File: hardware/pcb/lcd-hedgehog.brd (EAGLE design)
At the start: 24.4 x 27.4 mm, 22 parts

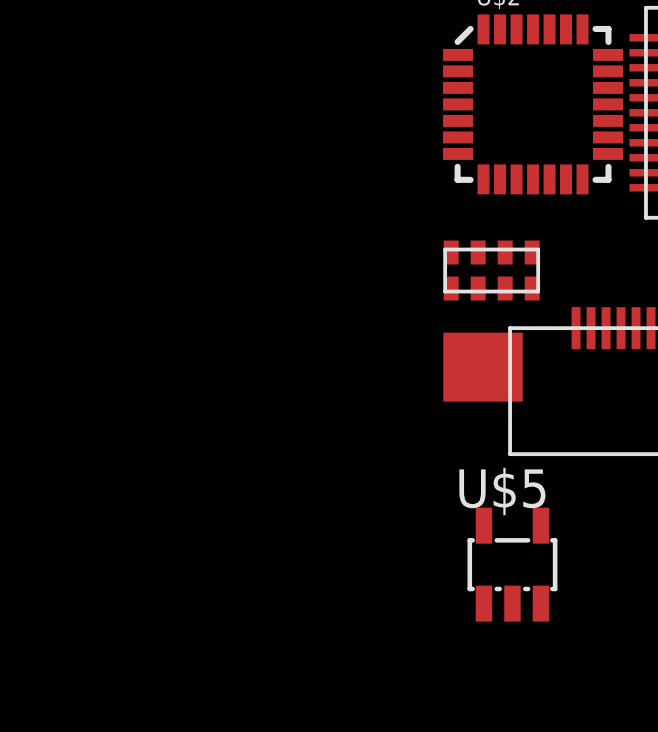
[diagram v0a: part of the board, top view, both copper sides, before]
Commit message: added ble
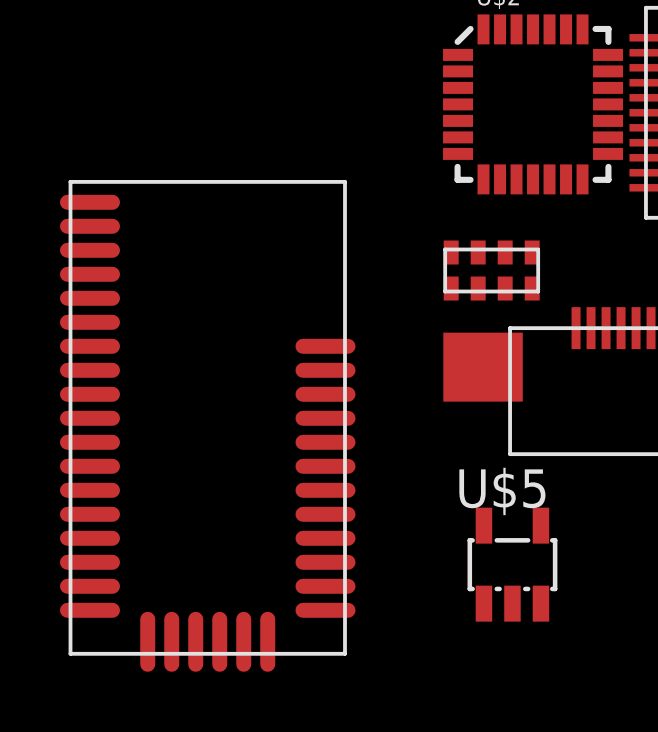
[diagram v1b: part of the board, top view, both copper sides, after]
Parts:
- added U$6: BLE113-A, jnode:BLE113-A
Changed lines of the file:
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@@
 <element name="U$4" library="HedgehogLib" package="SFV23" value="SFV23" x="2.1082" y="-12.6746"/>
 <element name="U$5" library="HedgehogLib" package="SOT-23-5" value="LM2703" x="-5.5118" y="-19.558"/>
+<element name="U$6" library="jnode" package="BLE113-A" value="BLE113-A" x="-20.2438" y="-22.5298"/>
 </elements>
 <signals>

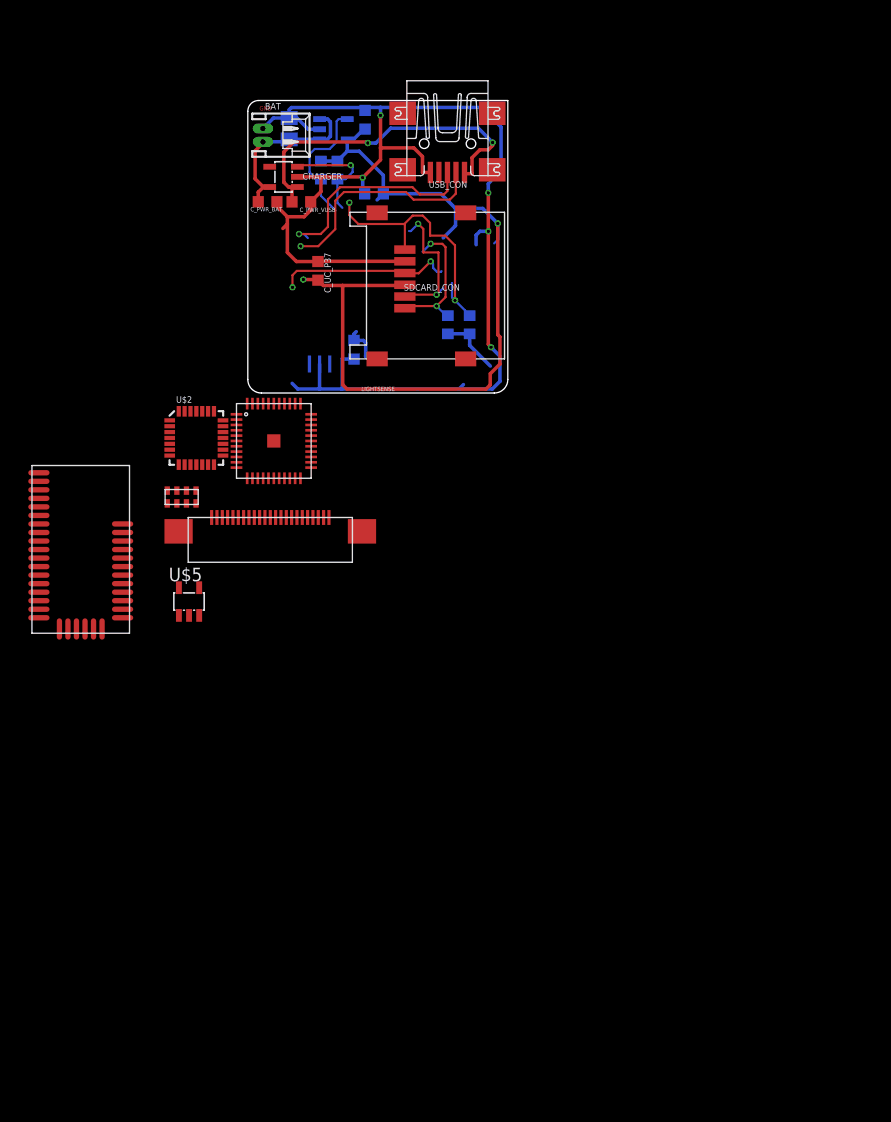
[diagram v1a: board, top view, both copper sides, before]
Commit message: added some wiring
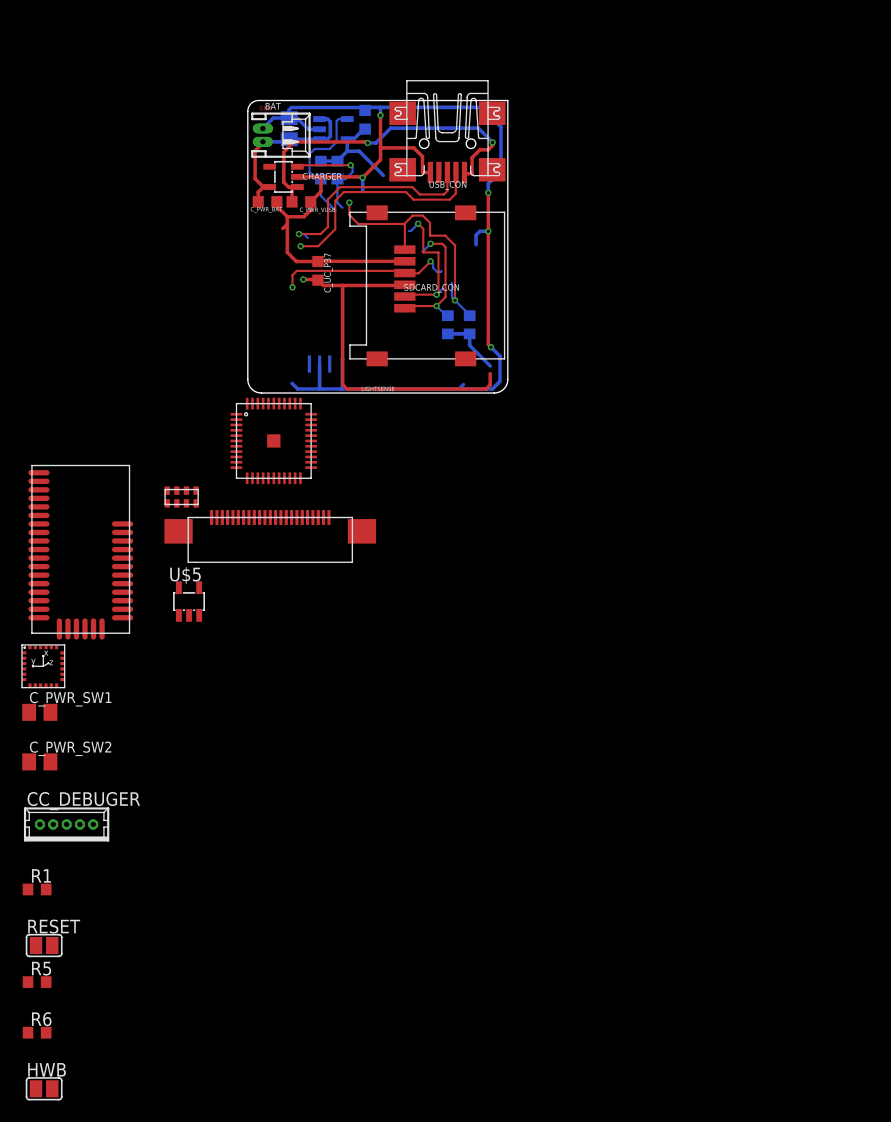
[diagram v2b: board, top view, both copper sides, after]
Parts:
- removed C_UC_P28/29, C_UC_P7/8: 0.22u, rcl:C0603K
- removed U$2: LSM303LGA28_LONG, jnode:LGA28
- added CC_DEBUGER: PROGCON, HedgehogLib:53047-05-OCT
- added C_PWR_SW1, C_PWR_SW2: 10u, rcl:C0805K
- added HWB, RESET: (no value), jumper:SJ
- added R1: 10k, rcl:R0603
- added R5, R6: 22, rcl:R0603
- added U$7: LSM9D, jnode:LGA4X4
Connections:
- removed net USB_D+@RC5: USB_CON.3
- removed net USB_D-@RC4: USB_CON.2
- new net BLE_RESET: CC_DEBUGER.2, U$6.P$34
- new net CS_SD: U$1.28
- new net D+: R5.2, USB_CON.3
- new net D-: R6.2, USB_CON.2
- new net MISO: U$1.11
- new net MOSI: U$1.10
- new net N$1: R1.1, RESET.2, U$1.13
- new net N$11: U$1.30
- new net N$2: 12MHZ_RESONATOR.2, U$1.17
- new net N$3: 12MHZ_RESONATOR.1, U$1.16
- new net N$4: HWB.1, U$1.33
- new net N$5: R6.1, U$1.3
- new net N$6: R5.1, U$1.4
- new net N$7: U$7.P$24
- new net P0_1/INT: U$1.29, U$6.P$32
- new net P0_4/TX: U$1.20, U$6.P$29
- new net P0_5/RX: U$1.21, U$6.P$28
- new net P2_1: CC_DEBUGER.4, U$6.P$10
- new net P2_2: CC_DEBUGER.3, U$6.P$9
- new net SCL: U$1.18, U$3.8
- new net SDA: U$1.19, U$3.1
- net +3V3: now also CC_DEBUGER.1, C_PWR_SW1.2, C_PWR_SW2.2, R1.2, U$1.14, U$1.24, U$1.34, U$1.44, U$3.5, U$6.P$17, U$6.P$8; no longer C_UC_P28/29.1, C_UC_P7/8.1
- net GND: now also CC_DEBUGER.5, C_PWR_SW1.1, C_PWR_SW2.1, HWB.2, RESET.1, U$1.15, U$1.23, U$1.35, U$1.43, U$1.45, U$1.5, U$1.6, U$3.3, U$4.P$2, U$5.2, U$6.P$1, U$6.P$18, U$6.P$2, U$6.P$25, U$6.P$3, U$6.P$36, U$6.P$4, U$6.P$5, U$6.P$6, U$6.P$7, U$7.P$5; no longer C_UC_P28/29.2, C_UC_P7/8.2
- net SCLK: now also U$1.9
- net V_USB: now also U$1.2, U$1.7
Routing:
- net +3V3: track 88.7 -> 50.6 mm, vias 2 -> 1
- net USB_D-@RC4: track 20.9 -> 0.00 mm, vias 1 -> 0
- net D-: track 0.00 -> 20.9 mm, vias 0 -> 1
- net USB_D+@RC5: track 20.4 -> 0.00 mm, vias 1 -> 0
- net D+: track 0.00 -> 20.4 mm, vias 0 -> 1
- net GND: track 128.1 -> 126.6 mm

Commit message: connected IMU
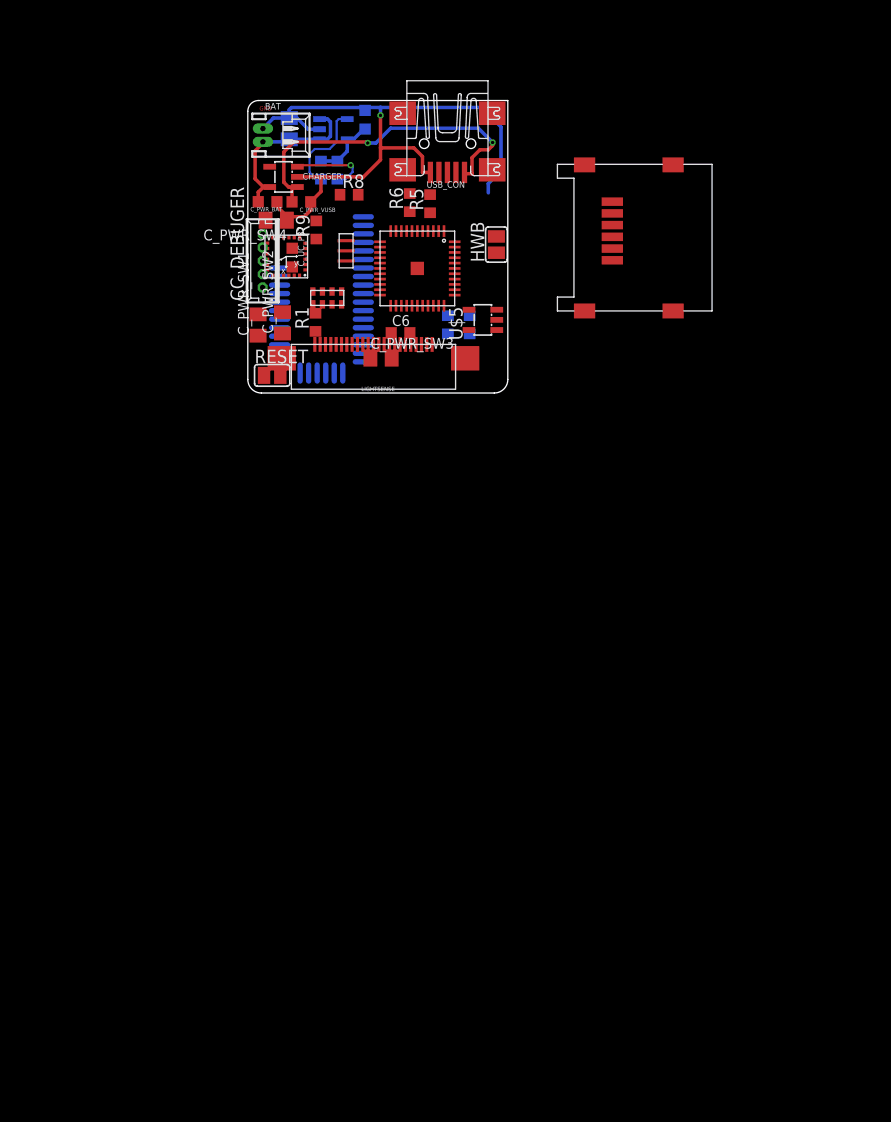
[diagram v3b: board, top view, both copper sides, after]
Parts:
- added C6: 1uF, rcl:C0603K
- added C_PWR_SW3: 4.7uF, rcl:C0805K
- added C_PWR_SW4: 0.22uF, rcl:C0805K
- added R8, R9: 3k3, rcl:R0603
- moved HWB 89.8 mm to (23.3, 13.9), turned to 90 degrees
- moved R6 85.3 mm to (15.2, 17.9), turned to 90 degrees
- moved R5 81.8 mm to (17.1, 17.8), turned to 90 degrees
- moved R1 59.3 mm to (6.35, 6.63), turned to 90 degrees
- moved RESET 57.6 mm to (2.29, 1.65)
- moved CC_DEBUGER 56.0 mm to (1.40, 12.4), turned to 90 degrees
- moved C_PWR_SW2 47.0 mm to (3.25, 6.58), turned to 90 degrees
- moved U$7 44.7 mm to (3.61, 12.8), turned to 180 degrees
- moved C_PWR_SW1 41.7 mm to (0.97, 6.38), turned to 90 degrees
- moved U$6 39.8 mm to (11.5, 1.47), flipped to the bottom
- moved U$5 38.2 mm to (22.0, 6.86), turned to 90 degrees
- moved U$3 23.7 mm to (7.90, 8.92), turned to 180 degrees
- moved U$1 21.0 mm to (15.9, 11.7), turned to 270 degrees
- moved SDCARD_CON 20.0 mm to (43.5, 7.70)
- moved U$4 18.9 mm to (11.8, 3.56)
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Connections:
- new net 3G_INT: U$1.30, U$7.P$13
- new net N$10: U$1.12
- new net N$8: C_PWR_SW4.2, U$7.P$9
- new net N$9: C_PWR_SW3.1, U$7.P$7
- net +3V3: now also R8.2, R9.2, U$7.P$10, U$7.P$15, U$7.P$18, U$7.P$19, U$7.P$20
- net GND: now also C6.2, C_PWR_SW3.2, U$7.P$22, U$7.P$23; no longer U$1.6
- net N$11: now also C6.1, U$1.6; no longer U$1.30
- net N$7: now also C_PWR_SW4.1, U$7.P$8; no longer U$7.P$24
- net SCL: now also R8.1, U$7.P$21
- net SDA: now also R9.1, U$7.P$24
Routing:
- net GND: track 126.6 -> 63.7 mm, vias 5 -> 1
- net +3V3: track 50.6 -> 6.03 mm, vias 1 -> 0
- net SDO: track 25.4 -> 0.00 mm, vias 2 -> 0
- net D-: track 20.9 -> 0.00 mm, vias 1 -> 0
- net D+: track 20.4 -> 0.00 mm, vias 1 -> 0
- net SCLK: track 16.6 -> 0.00 mm, vias 2 -> 0
- net SDI: track 13.4 -> 0.00 mm, vias 2 -> 0
- net CS_SDCARD: track 13.2 -> 0.00 mm, vias 2 -> 0
- net PWRGD: track 12.6 -> 9.08 mm
- net POK: track 10.4 -> 7.49 mm

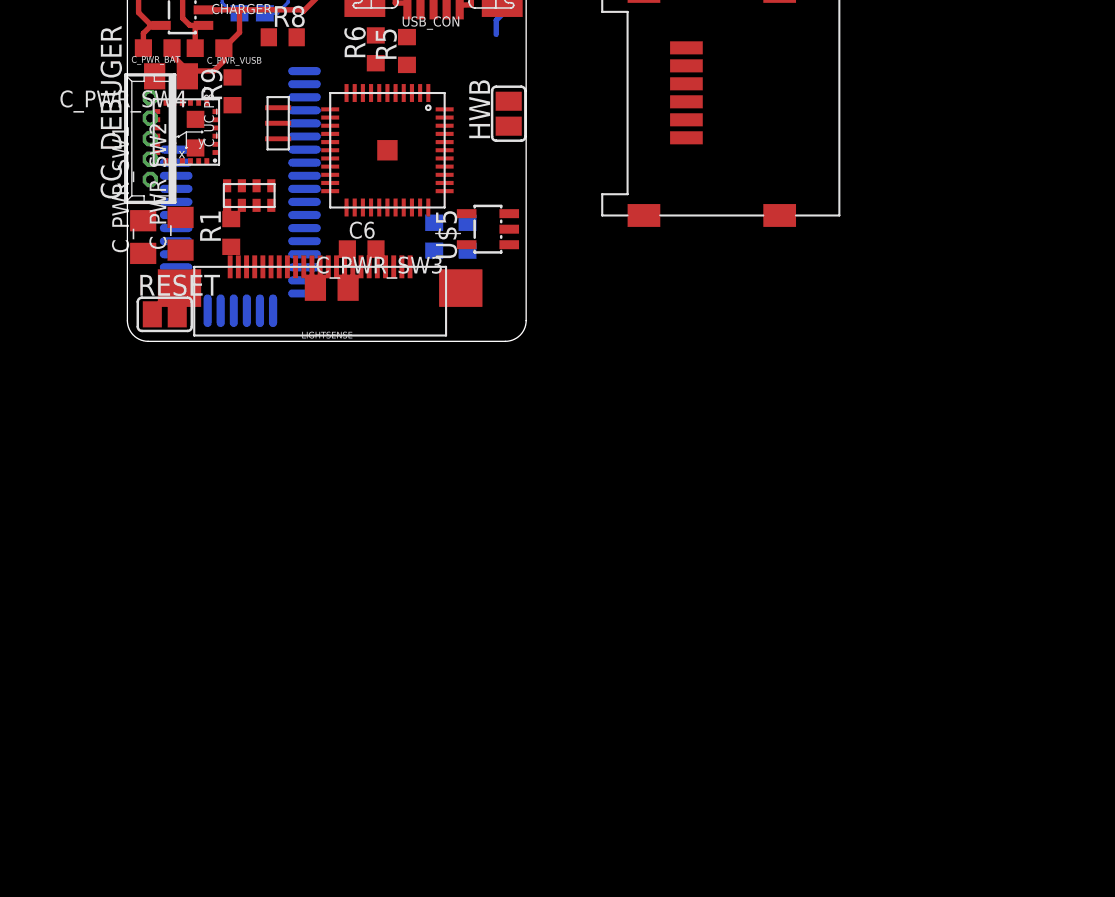
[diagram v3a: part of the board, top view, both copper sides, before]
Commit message: added Grid Eye
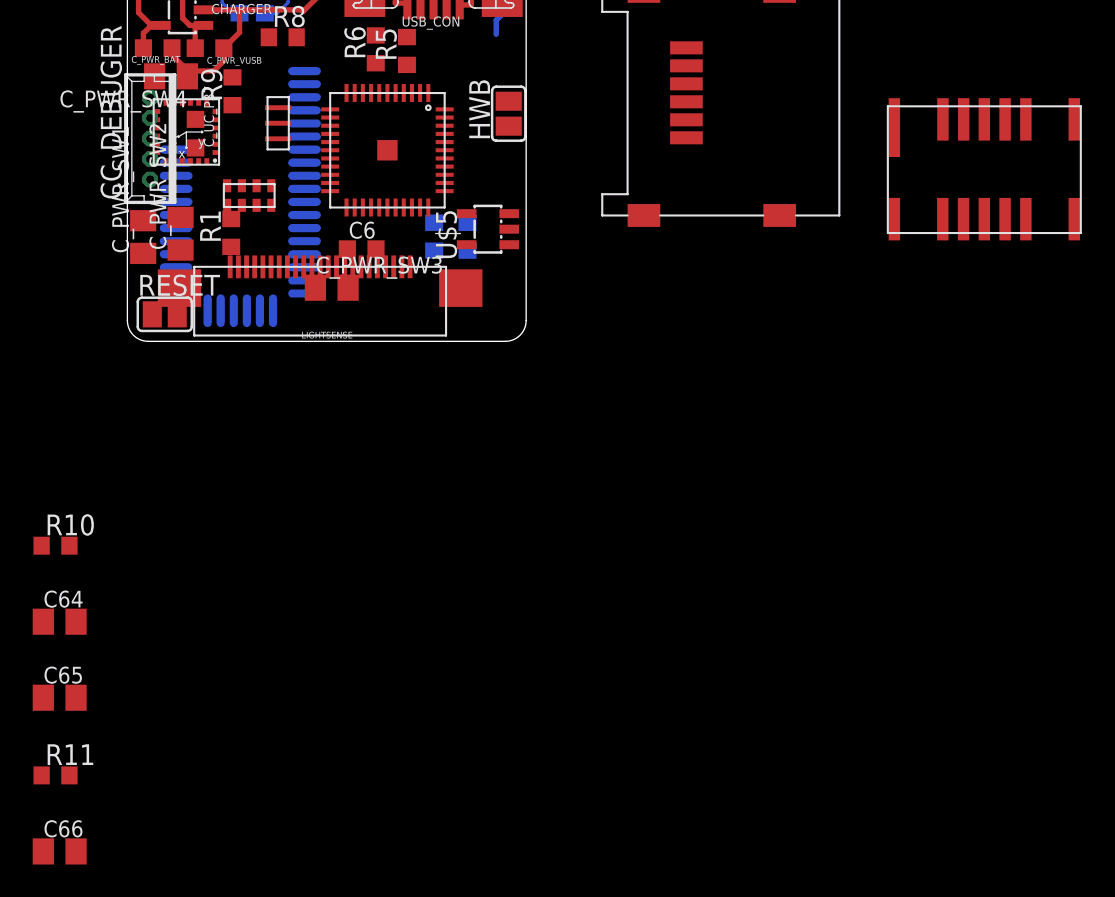
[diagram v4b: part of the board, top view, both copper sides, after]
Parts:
- added C64: 1.5uF, rcl:C0805K
- added C65: 1uF, rcl:C0805K
- added C66: 10uF, rcl:C0805K
- added R10: 10k, rcl:R0603
- added R11: 20, rcl:R0603
- added U$2: GRID-EYE, HedgehogLib:GRID-EYE
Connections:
- new net GRID_EYE_INT: R10.1, U$2.P4
- new net N$12: C64.1, U$2.P12
- new net N$13: C65.1, U$2.P10
- new net N$14: C65.2, R11.2
- net +3V3: now also C66.1, R10.2, U$2.P13, U$2.P9
- net GND: now also C64.2, C66.2, R11.1, U$2.P5, U$2.P6
- net SCL: now also U$2.P3
- net SDA: now also U$2.P2
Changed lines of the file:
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@@
 <?xml version="1.0" encoding="utf-8"?>
 <!DOCTYPE eagle SYSTEM "eagle.dtd">
-<eagle version="6.3">
+<eagle version="6.5.0">
 <drawing>
 <settings>
@@
 <element name="R8" library="rcl" package="R0603" value="3k3" x="9.4996" y="18.5928"/>
 <element name="R9" library="rcl" package="R0603" value="3k3" x="6.4262" y="15.2908" rot="R90"/>
+<element name="U$2" library="HedgehogLib" package="GRID-EYE" value="GRID-EYE" x="52.4002" y="6.1722"/>
+<element name="R10" library="rcl" package="R0603" value="10k" x="-4.3942" y="-12.4968"/>
+<element name="C64" library="rcl" package="C0805K" value="1.5uF" x="-4.1402" y="-17.145"/>
+<element name="C65" library="rcl" package="C0805K" value="1uF" x="-4.1402" y="-21.7932"/>
+<element name="R11" library="rcl" package="R0603" value="20" x="-4.3942" y="-26.543"/>
+<element name="C66" library="rcl" package="C0805K" value="10uF" x="-4.1402" y="-31.1912"/>
 </elements>
 <signals>
@@
 <contactref element="C_PWR_SW3" pad="2"/>
 <contactref element="C6" pad="2"/>
+<contactref element="U$2" pad="P5"/>
+<contactref element="U$2" pad="P6"/>
+<contactref element="R11" pad="1"/>
+<contactref element="C64" pad="2"/>
+<contactref element="C66" pad="2"/>
 <wire x1="23.3172" y1="14.6812" x2="34.1856" y2="16.8462" width="0" layer="19" extent="1-1"/>
 <wire x1="19.4004" y1="13.684" x2="23.3172" y2="14.6812" width="0" layer="19" extent="1-1"/>
@@
 <wire x1="2.9808" y1="2.9232" x2="3.2512" y2="5.5786" width="0" layer="19" extent="1-16"/>
 <wire x1="1.524" y1="1.651" x2="2.9808" y2="2.9232" width="0" layer="19" extent="1-16"/>
+<wire x1="53.6702" y1="13.5722" x2="1.524" y2="1.651" width="0" layer="19" extent="1-1"/>
+<wire x1="54.9402" y1="13.5722" x2="53.6702" y2="13.5722" width="0" layer="19" extent="1-1"/>
 <wire x1="23.3473" y1="6.858" x2="19.4004" y2="9.684" width="0" layer="19" extent="1-1"/>
+<wire x1="-3.1402" y1="-17.145" x2="53.6702" y2="13.5722" width="0" layer="19" extent="1-1"/>
+<wire x1="-5.2442" y1="-26.543" x2="-3.1402" y2="-17.145" width="0" layer="19" extent="1-1"/>
+<wire x1="-3.1402" y1="-31.1912" x2="-5.2442" y2="-26.543" width="0" layer="19" extent="1-1"/>
 </signal>
 <signal name="D+">
@@
 <contactref element="R8" pad="2"/>
 <contactref element="R9" pad="2"/>
+<contactref element="R10" pad="2"/>
+<contactref element="U$2" pad="P13"/>
+<contactref element="C66" pad="1"/>
+<contactref element="U$2" pad="P9"/>
 <wire x1="19.4004" y1="14.184" x2="34.1856" y2="14.6462" width="0" layer="19" extent="1-1"/>
 <wire x1="19.4004" y1="9.184" x2="19.4004" y2="14.184" width="0" layer="19" extent="1-1"/>
@@
 <wire x1="10.3496" y1="18.5928" x2="6.4262" y2="16.1408" width="0" layer="19" extent="1-1"/>
 <wire x1="8.4074" y1="21.7542" x2="10.3496" y2="18.5928" width="0" layer="19" extent="1-16"/>
+<wire x1="54.9402" y1="7.4722" x2="10.8308" y2="3.7232" width="0" layer="19" extent="1-16"/>
+<wire x1="49.8602" y1="7.4722" x2="54.9402" y2="7.4722" width="0" layer="19" extent="1-1"/>
+<wire x1="-3.5442" y1="-12.4968" x2="49.8602" y2="7.4722" width="0" layer="19" extent="1-1"/>
+<wire x1="-5.1402" y1="-31.1912" x2="-3.5442" y2="-12.4968" width="0" layer="19" extent="1-1"/>
 </signal>
 <signal name="SDI">
@@
 <contactref element="U$7" pad="P$24"/>
 <contactref element="R9" pad="1"/>
+<contactref element="U$2" pad="P2"/>
 <wire x1="8.7994" y1="9.5154" x2="12.4004" y2="10.684" width="0" layer="19" extent="1-1"/>
 <wire x1="4.8568" y1="11.0266" x2="8.7994" y2="9.5154" width="0" layer="19" extent="1-1"/>
 <wire x1="6.4262" y1="14.4408" x2="4.8568" y2="11.0266" width="0" layer="19" extent="1-1"/>
+<wire x1="49.8702" y1="13.5722" x2="4.8568" y2="11.0266" width="0" layer="19" extent="1-1"/>
 </signal>
 <signal name="SCL">
@@
 <contactref element="U$7" pad="P$21"/>
 <contactref element="R8" pad="1"/>
+<contactref element="U$2" pad="P3"/>
 <wire x1="12.4004" y1="11.184" x2="8.6496" y2="18.5928" width="0" layer="19" extent="1-1"/>
 <wire x1="8.7994" y1="8.3154" x2="12.4004" y2="11.184" width="0" layer="19" extent="1-1"/>
 <wire x1="3.3568" y1="11.0266" x2="8.7994" y2="8.3154" width="0" layer="19" extent="1-1"/>
+<wire x1="51.1402" y1="13.5722" x2="3.3568" y2="11.0266" width="0" layer="19" extent="1-1"/>
 </signal>
 <signal name="MOSI">
@@
 <wire x1="13.4506" y1="5.6388" x2="15.9004" y2="15.184" width="0" layer="19" extent="1-1"/>
 </signal>
+<signal name="GRID_EYE_INT">
+<contactref element="U$2" pad="P4"/>
+<contactref element="R10" pad="1"/>
+<wire x1="52.4002" y1="13.5722" x2="-5.2442" y2="-12.4968" width="0" layer="19" extent="1-1"/>
+</signal>
+<signal name="N$12">
+<contactref element="U$2" pad="P12"/>
+<contactref element="C64" pad="1"/>
+<wire x1="51.1302" y1="7.4722" x2="-5.1402" y2="-17.145" width="0" layer="19" extent="1-1"/>
+</signal>
+<signal name="N$13">
+<contactref element="U$2" pad="P10"/>
+<contactref element="C65" pad="1"/>
+<wire x1="53.6702" y1="7.4722" x2="-5.1402" y2="-21.7932" width="0" layer="19" extent="1-1"/>
+</signal>
+<signal name="N$14">
+<contactref element="C65" pad="2"/>
+<contactref element="R11" pad="2"/>
+<wire x1="-3.1402" y1="-21.7932" x2="-3.5442" y2="-26.543" width="0" layer="19" extent="1-1"/>
+</signal>
 </signals>
